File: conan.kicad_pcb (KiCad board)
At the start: 4 copper layers, 313 parts, among them J1 JST-XH, J10 PWM11, J11 PWM3, J12 PWM7, J13 PWM12, J14 PWM4, J15 PWM8, J16 Stepper, J17 Stepper, J18 Stepper, J19 Stepper, J2 JST-XH, J20 Stepper, J21 Stepper, J22 Boot, J23 UART1, J24 UART2, J25 USB_B_Micro, J26 Endstop 1, J27 Endstop 2, J28 Endstop 3, J29 Endstop 4, J3 JTAG, J30 Endstop 5, J31 Endstop 6, J32 Endstop 7, J33 Endstop 8, J34 Watchdog, J35 Thermistor 1, J36 Thermistor 2, J37 Thermistor 3, J38 Thermistor 4, J39 Thermistor 5, J4 PWM9, J40 Thermistor 6, J43 pmod, J44 esp8266, J45 Chain_in, J46 Chain_out, J47 Exp1_L, J48 Display, J49 Exp1_R, J5 PWM5, J50 Vaux in, J51 VM2 in, J52 VM1 in, J53 Vaux in, J54 Exp2_L, J55 Exp2_R, J6 PWM1_HP, J7 PWM10, J8 PWM2_HP, J9 PWM6, Q1 AON7524, Q2 TPH1R405PL, Q3 TPH1R405PL, Q4 AON7524, Q5 AON7524, Q6 AON7524, Q7 AON7524, Q8 AON7524, Q9 Q_NMOS_DGS, SW1 Reset, U1 ECP5U12_CABGA256, U10 TMC2209, U11 TMC2209, U12 TMC2209, U13 TMC2209, U14 AT25xxx, U15 STM32F070CBTx, U16 74VLX244, U17 STWD100, U2 L7986, U3 TLV62569, U4 TLV62569, U5 LP5907MFX-2.5, U6 LP5907MFX-3.3, U7 MIC4127, U8 TMC2209, U9 TMC2209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

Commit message: placement roughly done
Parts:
- J44: value esp8266 -> ESP8266
- Y1: value 8MHz -> 16MHz; footprint arne:crystal_ecs-5px -> Crystal:Crystal_SMD_SeikoEpson_TSX3225-4Pin_3.2x2.5mm
- moved J34 173.3 mm to (194.8, 28.2), turned to 180 degrees
- moved Q9 126.6 mm to (186.6, 26.7), turned to 270 degrees
- moved R65 120.1 mm to (185.7, 30.4), turned to 0 degrees
- moved R66 116.3 mm to (181.1, 31.0), turned to 0 degrees
- moved R67 113.1 mm to (181.6, 27.4), turned to 180 degrees
- moved U17 110.2 mm to (180.5, 35.5), turned to 0 degrees
- moved TH2 75.9 mm to (88.3, 36.4)
- moved TH1 75.9 mm to (164.2, 36.4)
- moved R56 63.0 mm to (65.8, 52.6)
- moved R55 61.9 mm to (62.8, 52.7)
- moved J25 61.1 mm to (53.8, 60.0), turned to 270 degrees
- moved R83 58.1 mm to (97.7, 63.7), turned to 90 degrees
- moved U15 58.0 mm to (66.7, 59.7), turned to 180 degrees
- moved R50 56.0 mm to (73.8, 62.1), turned to 270 degrees
- moved J23 55.7 mm to (82.3, 82.8), turned to 270 degrees
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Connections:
- J44 pad 2: ESP_EN -> GND
- J44 pad 3: ESP_RST -> ESP_EN
- J44 pad 4: +3V3 -> ESP_GPIO2
- J44 pad 5: ESP_RX -> ESP_RST
- J44 pad 7: ESP_GPIO2 -> +3V3
- J44 pad 8: GND -> ESP_RX
- U1 pad A13: CLK_50MHz -> display3
- U1 pad A7: display3 -> CLK_50MHz
- U1 pad C8: Net-(U1-PadC8) -> CLK_48MHz
- U15 pad 29: Net-(U15-Pad29) -> CLK_48MHz
- Y1 pad 2: Net-(C88-Pad1) -> GND
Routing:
- net CLK: track 135.9 -> 191.9 mm, vias 9 -> 10
- net DIR1: track 17.3 -> 73.2 mm
- net STEP1: track 17.7 -> 72.6 mm
- net INDEX1: track 19.3 -> 72.2 mm, vias 2 -> 3
- net DIAG1: track 18.0 -> 70.8 mm, vias 1 -> 2
- net ENN: track 177.8 -> 230.4 mm
- net UART2: track 3.77 -> 54.9 mm, vias 1 -> 2
- net DIR2: track 19.5 -> 69.8 mm, vias 2 -> 3
- net UART1: track 3.17 -> 52.4 mm, vias 0 -> 1
- net ADC6: track 13.8 -> 61.7 mm, vias 1 -> 2
- net exp2_17: track 2.20 -> 48.1 mm
- net exp2_16: track 3.33 -> 47.6 mm
- net exp2_14: track 4.90 -> 47.6 mm
- net exp2_15: track 2.20 -> 44.9 mm
- net exp2_13: track 2.20 -> 44.2 mm
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
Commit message: routing snapshot
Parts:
- moved R12 7.28 mm to (122.3, 57.4)
- moved X1 5.56 mm to (126.2, 56.5), turned to 180 degrees
- moved J48 2.45 mm to (111.1, 49.1)
- moved C49 1.05 mm to (126.2, 53.7), turned to 180 degrees
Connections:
- U1 pad A7: CLK_50MHz -> CLK_48MHz
- U1 pad C8: CLK_48MHz -> CLK_50MHz
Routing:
- net display6: track 3.17 -> 44.6 mm
- net display2: track 3.17 -> 24.0 mm
- net display8: track 4.73 -> 25.0 mm
- net display10: track 2.20 -> 21.8 mm
- net display4: track 3.77 -> 23.2 mm
- net display12: track 4.73 -> 23.8 mm
- net CLK_48MHz: track 3.91 -> 21.2 mm, vias 0 -> 2
- net display9: track 2.20 -> 19.1 mm
- net display7: track 3.77 -> 20.6 mm
- net display1: track 2.20 -> 19.0 mm
- net display3: track 2.20 -> 18.8 mm
- net display11: track 3.17 -> 19.4 mm
- net display5: track 4.73 -> 21.0 mm
- net display13: track 3.77 -> 19.5 mm
- net CLK_50MHz: track 2.20 -> 16.8 mm
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
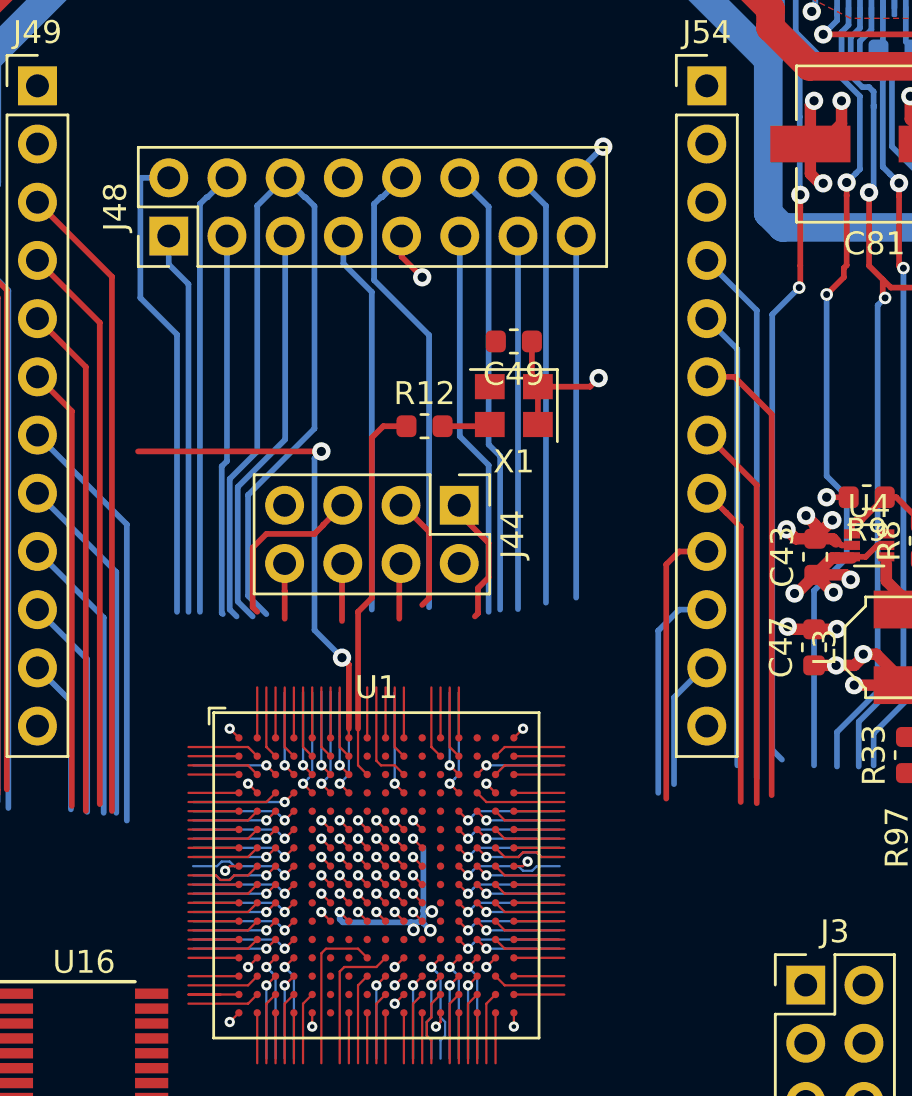
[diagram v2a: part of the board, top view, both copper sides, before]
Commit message: reassign some FPGA pins for ease of routing
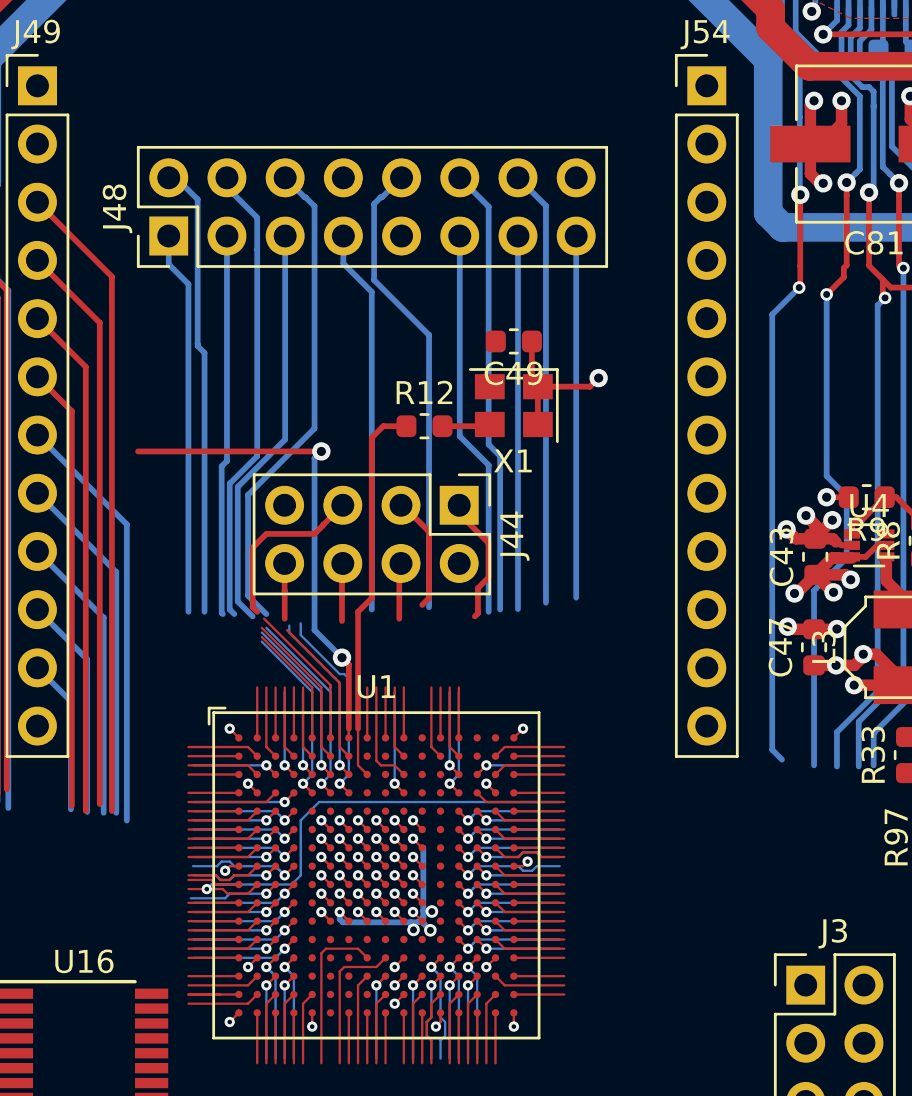
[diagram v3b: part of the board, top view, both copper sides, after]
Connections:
- U1 pad A10: chain_in_in3 -> ESP_TX
- U1 pad A12: ESP_FLASH -> display10
- U1 pad A13: display3 -> exp2_1
- U1 pad A5: display10 -> display2
- U1 pad A6: display9 -> display5
- U1 pad A8: display1 -> ESP_FLASH
- U1 pad A9: chain_in_in1 -> ESP_GPIO2
- U1 pad B10: chain_in_in2 -> ESP_EN
- U1 pad B12: ESP_GPIO2 -> display9
- U1 pad B13: ESP_EN -> display11
- U1 pad B15: exp2_12 -> exp2_2
- U1 pad B16: exp2_13 -> exp2_3
- U1 pad B5: display11 -> Net-(U1-PadB5)
- U1 pad B6: display6 -> display3
- U1 pad B7: display2 -> ESP_RST
- U1 pad C10: chain_in_out1 -> display7
- U1 pad C13: ESP_RX -> display12
- U1 pad C14: exp2_11 -> exp2_5
- U1 pad C15: exp2_7 -> exp2_4
- U1 pad C16: exp2_9 -> exp2_6
- U1 pad C5: display13 -> Net-(U1-PadC5)
- U1 pad C6: display7 -> Net-(U1-PadC6)
- U1 pad C7: display4 -> display6
- U1 pad D10: chain_in_out2 -> display8
- U1 pad D13: ESP_RST -> display13
- U1 pad D14: exp2_10 -> exp2_8
- U1 pad D16: exp2_5 -> exp2_7
- U1 pad D5: display12 -> display1
- U1 pad D6: display8 -> display4
- U1 pad D7: display5 -> ESP_RX
- U1 pad E13: ESP_TX -> STEP4
- U1 pad E14: exp2_8 -> INDEX4
- U1 pad E15: exp2_3 -> DIAG4
- U1 pad E16: DIAG6 -> DIR4
- U1 pad F13: exp2_4 -> Net-(U1-PadF13)
- U1 pad F14: exp2_6 -> Net-(U1-PadF14)
- U1 pad F15: exp2_2 -> Net-(U1-PadF15)
- U1 pad G13: exp2_1 -> Net-(U1-PadG13)
- U1 pad H14: DIAG4 -> Net-(U1-PadH14)
- U1 pad J13: INDEX4 -> Net-(U1-PadJ13)
- U1 pad J15: DIR4 -> Net-(U1-PadJ15)
- U1 pad K15: STEP4 -> Net-(U1-PadK15)
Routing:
- net exp2_1: track 28.2 -> 2.20 mm, vias 1 -> 0
- net exp2_3: track 23.3 -> 2.20 mm
- net exp2_2: track 23.2 -> 3.17 mm
- net exp2_4: track 21.7 -> 3.17 mm, vias 1 -> 0
- net CLK: track 191.9 -> 210.4 mm, vias 10 -> 11
- net display6: track 44.6 -> 28.7 mm, vias 0 -> 1
- net exp2_6: track 16.0 -> 2.20 mm, vias 1 -> 0
- net exp2_5: track 16.3 -> 3.77 mm, vias 0 -> 1
- net exp2_7: track 12.7 -> 2.20 mm
- net Net-(U1-PadC6): track 0.00 -> 7.44 mm, vias 0 -> 1
- net display1: track 19.0 -> 24.6 mm, vias 0 -> 1
- net display4: track 23.2 -> 28.9 mm
- net exp2_8: track 9.49 -> 3.97 mm, vias 1 -> 0
- net ESP_RX: track 6.18 -> 11.1 mm
- net Net-(U1-PadG13): track 0.00 -> 4.73 mm, vias 0 -> 1
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
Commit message: more routing
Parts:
- moved R45 29.5 mm to (161.9, 51.9)
- moved R97 24.2 mm to (147.7, 51.4)
- moved R48 24.1 mm to (150.4, 51.4)
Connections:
- U1 pad A5: display2 -> display1
- U1 pad C6: Net-(U1-PadC6) -> display2
- U1 pad D5: display1 -> Net-(U1-PadD5)
- U1 pad J2: CLK -> exp1_12
- U1 pad J4: exp1_12 -> CLK
- U1 pad K2: ENN -> PWM5
- U1 pad K4: PWM5 -> ENN
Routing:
- net UART6: track 4.90 -> 49.6 mm, vias 1 -> 2
- net ENN: track 230.4 -> 266.7 mm, vias 10 -> 13
- net UART5: track 2.20 -> 36.2 mm, vias 0 -> 1
- net Net-(R45-Pad2): track 48.6 -> 19.0 mm, vias 4 -> 3
- net exp2_1: track 2.20 -> 25.3 mm
- net Net-(R48-Pad2): track 37.6 -> 15.1 mm, vias 4 -> 3
- net Net-(R97-Pad2): track 42.7 -> 20.4 mm, vias 4 -> 3
- net exp2_2: track 3.17 -> 23.3 mm
- net UART4: track 3.77 -> 23.3 mm, vias 1 -> 2
- net exp2_3: track 2.20 -> 20.3 mm
- net STEP6: track 52.0 -> 69.1 mm
- net exp2_4: track 3.17 -> 20.2 mm
- net DIAG6: track 49.5 -> 66.4 mm
- net DIR6: track 54.3 -> 71.1 mm
- net INDEX6: track 50.3 -> 66.9 mm
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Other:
- net class Default: clearance 0.1 -> 0.15
- rule trace_clearance: 0.1 -> 0.15

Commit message: more routing
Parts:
- Q1: footprint Package_DFN_QFN:DFN-8-1EP_3x3mm_P0.5mm_EP1.66x2.38mm -> arne:FET_DGS_DFN3x3A_8L_EP1_P
- moved R95 87.4 mm to (196.6, 86.8)
- moved R86 80.1 mm to (117.2, 90.7)
- moved R25 10.4 mm to (134.3, 93.4), turned to 90 degrees
- moved J3 9.58 mm to (132.2, 88.5), turned to 90 degrees
- moved JP3 9.08 mm to (165.3, 88.0), turned to 270 degrees
- moved R13 7.27 mm to (161.4, 91.5), turned to 90 degrees
- moved JP2 6.59 mm to (123.1, 93.0)
- moved R29 5.75 mm to (185.2, 76.4), turned to 90 degrees
- moved JP4 5.51 mm to (142.3, 93.0)
- moved R19 5.37 mm to (171.6, 92.2), turned to 90 degrees
- moved R21 4.73 mm to (176.4, 73.8), turned to 0 degrees
- moved R17 4.44 mm to (130.8, 93.4), turned to 90 degrees
- moved R30 4.32 mm to (189.3, 92.3), turned to 90 degrees
- moved R28 4.26 mm to (150.7, 93.5), turned to 90 degrees
- moved J10 4.15 mm to (146.7, 98.6), turned to 180 degrees
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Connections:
- U1 pad F13: Net-(U1-PadF13) -> DIR5
- U1 pad F14: Net-(U1-PadF14) -> INDEX5
- U1 pad F15: Net-(U1-PadF15) -> STEP5
- U1 pad F16: INDEX6 -> UART5
- U1 pad G13: Net-(U1-PadG13) -> UART6
- U1 pad G14: DIAG5 -> STEP6
- U1 pad G15: INDEX5 -> DIR6
- U1 pad G16: UART5 -> DIAG5
- U1 pad H13: UART6 -> INDEX6
- U1 pad H14: Net-(U1-PadH14) -> exp2_17
- U1 pad H15: DIR6 -> DIAG6
- U1 pad J13: Net-(U1-PadJ13) -> exp2_12
- U1 pad J15: Net-(U1-PadJ15) -> exp2_15
- U1 pad J16: DIR5 -> exp2_16
- U1 pad K13: pmod1_4 -> exp2_11
- U1 pad K14: STEP6 -> exp2_10
- U1 pad K15: Net-(U1-PadK15) -> exp2_13
- U1 pad K16: STEP5 -> exp2_14
- U1 pad L1: PWM1 -> Net-(U1-PadL1)
- U1 pad L13: pmod1_3 -> exp2_9
- U1 pad L14: pmod1_1 -> PWM2
- U1 pad L16: pmod2_1 -> PWM1
- U1 pad M1: PWM2 -> Net-(U1-PadM1)
- U1 pad N12: exp2_14 -> Net-(U1-PadN12)
- U1 pad R12: exp2_16 -> Net-(U1-PadR12)
- U1 pad T13: exp2_15 -> Net-(U1-PadT13)
- U1 pad T14: exp2_17 -> Net-(U1-PadT14)
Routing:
- net PWM2: track 5.41 -> 75.8 mm, vias 0 -> 2
- net PWM1: track 5.49 -> 72.4 mm, vias 0 -> 2
- net PWM4: track 3.17 -> 52.1 mm, vias 0 -> 2
- net +3V3: track 35.2 -> 83.6 mm, vias 24 -> 26
- net PWM3: track 3.17 -> 42.6 mm, vias 0 -> 2
- net exp2_11: track 38.5 -> 70.7 mm, vias 0 -> 1
- net exp2_9: track 35.8 -> 67.5 mm, vias 0 -> 1
- net exp2_12: track 40.7 -> 72.1 mm, vias 0 -> 1
- net exp2_10: track 36.3 -> 67.5 mm, vias 0 -> 1
- net exp2_13: track 42.0 -> 71.7 mm, vias 0 -> 1
- net exp2_15: track 44.9 -> 74.0 mm, vias 0 -> 1
- net GND: track 291.2 -> 320.0 mm, vias 119 -> 142
- net exp2_16: track 47.6 -> 74.0 mm, vias 0 -> 1
- net exp2_14: track 47.6 -> 72.0 mm
- net +2V5: track 35.1 -> 15.2 mm, vias 10 -> 7
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- added copper zone on In1.Cu, net GND
- added copper zone on In2.Cu, net Net-(J10-Pad3)
- added copper zone on F.Cu, net Net-(J11-Pad1)
- added copper zone on F.Cu, net Net-(J12-Pad1)
- added copper zone on In2.Cu, net Net-(J12-Pad2)
- added copper zone on F.Cu, net Net-(J14-Pad1)
- added copper zone on F.Cu, net Net-(J15-Pad1)
- added copper zone on In2.Cu, net Net-(J4-Pad3)
- added copper zone on F.Cu, net Net-(J5-Pad1)
- added copper zone on F.Cu, net Net-(J9-Pad1)

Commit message: power routing done
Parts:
- C48: moved to B.Cu
- moved R11 40.2 mm to (72.1, 64.8)
- moved R10 39.4 mm to (75.4, 64.8)
- moved J35 38.0 mm to (61.7, 77.5)
- moved J40 37.8 mm to (99.5, 77.5)
- moved J24 35.2 mm to (54.6, 52.0), turned to 180 degrees
- moved J23 29.9 mm to (54.5, 71.9), turned to 180 degrees
- moved R53 26.2 mm to (50.2, 49.9)
- moved J36 23.0 mm to (69.2, 77.5)
- moved JP11 22.6 mm to (74.6, 92.3), turned to 270 degrees
- moved J39 22.6 mm to (91.8, 77.5)
- moved R54 21.6 mm to (51.0, 53.3)
- moved C48 17.4 mm to (71.4, 59.5), turned to 270 degrees
- moved R88 13.0 mm to (57.8, 80.6)
- moved R92 12.5 mm to (107.4, 91.1), turned to 90 degrees
- moved R89 12.5 mm to (57.8, 82.7)
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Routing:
- net +3V3: track 83.6 -> 180.1 mm, vias 26 -> 38
- net Net-(J26-Pad1): track 0.00 -> 86.4 mm
- net +5V: track 47.6 -> 124.9 mm, vias 14 -> 22
- net CLK_48MHz: track 21.2 -> 86.1 mm, vias 2 -> 6
- net WDEN: track 2.20 -> 65.8 mm, vias 0 -> 2
- net WDI: track 2.28 -> 60.2 mm, vias 0 -> 2
- net chain_out_in2: track 3.17 -> 58.3 mm
- net chain_out_in1: track 3.77 -> 58.5 mm
- net chain_out_out1: track 2.20 -> 55.5 mm, vias 0 -> 1
- net Net-(J30-Pad3): track 0.00 -> 51.8 mm
- net chain_out_out2: track 4.73 -> 56.2 mm, vias 1 -> 2
- net chain_out_out3: track 2.20 -> 53.0 mm, vias 0 -> 1
- net Net-(J26-Pad3): track 0.00 -> 50.6 mm
- net FPGA2: track 4.73 -> 54.3 mm, vias 1 -> 2
- net FPGA3: track 3.60 -> 51.9 mm, vias 0 -> 1
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- added copper zone on F.Cu, net Net-(J34-Pad1)
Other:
- net class Default: clearance 0.15 -> 0.1
- rule trace_clearance: 0.15 -> 0.1

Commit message: more routing
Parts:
- added REF**: MountingHole_3.2mm_M3, MountingHole:MountingHole_3.2mm_M3, F.Cu at (200.9, 97.5)
- added REF**: MountingHole_3.2mm_M3, MountingHole:MountingHole_3.2mm_M3, F.Cu at (54.4, 97.5)
- added REF**: MountingHole_3.2mm_M3, MountingHole:MountingHole_3.2mm_M3, F.Cu at (54.4, 27.7)
- added REF**: MountingHole_3.2mm_M3, MountingHole:MountingHole_3.2mm_M3, F.Cu at (119.7, 41.0)
- added REF**: MountingHole_3.2mm_M3, MountingHole:MountingHole_3.2mm_M3, F.Cu at (200.9, 27.7)
- moved R75 95.9 mm to (193.3, 29.5)
- moved D11 95.4 mm to (193.4, 26.0)
- moved C1 79.2 mm to (128.0, 7.49)
- moved C10 79.2 mm to (124.0, 8.47)
- moved C13 79.2 mm to (119.4, 13.6)
- moved C18 79.2 mm to (128.0, 11.1)
- moved C20 79.2 mm to (122.5, 18.2)
- moved C22 79.2 mm to (124.0, 11.6)
- moved C23 79.2 mm to (117.9, 19.2)
- moved C25 79.2 mm to (123.0, 14.6)
- moved C4 79.2 mm to (119.9, 10.0)
- moved C7 79.2 mm to (118.4, 16.1)
- moved R72 59.6 mm to (183.7, 57.7), turned to 270 degrees
- moved R69 58.8 mm to (113.7, 58.9), turned to 180 degrees
- moved D5 53.5 mm to (112.7, 61.8), turned to 90 degrees
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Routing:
- net LED8: track 2.20 -> 99.3 mm, vias 0 -> 2
- net +3V3: track 180.1 -> 237.3 mm, vias 38 -> 42
- net LED5: track 3.17 -> 55.0 mm, vias 0 -> 1
- net /mcu/TX: track 0.00 -> 28.0 mm, vias 0 -> 1
- net Net-(R53-Pad1): track 0.00 -> 22.0 mm, vias 0 -> 2
- net Net-(C89-Pad1): track 16.9 -> 37.3 mm, vias 0 -> 2
- net LED4: track 3.17 -> 19.6 mm
- net Net-(D8-Pad2): track 0.00 -> 15.8 mm, vias 0 -> 2
- net Net-(J23-Pad2): track 0.00 -> 13.4 mm, vias 0 -> 2
- net Net-(J23-Pad3): track 0.00 -> 12.9 mm, vias 0 -> 2
- net GND: track 366.5 -> 377.8 mm, vias 164 -> 166
- net Net-(R55-Pad2): track 2.25 -> 10.3 mm
- net LED3: track 3.77 -> 11.7 mm
- net /mcu/RX: track 0.00 -> 7.85 mm
- net LED6: track 2.20 -> 9.01 mm
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
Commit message: more routing
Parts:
- removed C10, C11, C13, C16, C19, C8: 10nF, Capacitor_SMD:C_0603_1608Metric
- removed C28, C31, C33, C34, C9, C95: 100nF, Capacitor_SMD:C_0603_1608Metric
- removed REF** (x5): MountingHole_3.2mm_M3, MountingHole:MountingHole_3.2mm_M3
- added H1: MountingHole, MountingHole:MountingHole_3.2mm_M3, F.Cu at (54.4, 27.9)
- added H2: MountingHole, MountingHole:MountingHole_3.2mm_M3, F.Cu at (200.9, 27.9)
- added H3: MountingHole, MountingHole:MountingHole_3.2mm_M3, F.Cu at (54.4, 97.5)
- added H4: MountingHole, MountingHole:MountingHole_3.2mm_M3, F.Cu at (200.9, 97.5)
- added H5: MountingHole, MountingHole:MountingHole_3.2mm_M3, F.Cu at (119.7, 41.0)
- C1, C14, C15, C18, C2, C20, C21, C22, C23, C24, C25, C26, C27, C3, C30, C35, C4, C5, C6, C7: footprint Capacitor_SMD:C_0603_1608Metric -> Capacitor_SMD:C_0402_1005Metric; moved to B.Cu
- C12, C17, C36, C92, C93, C94, C96, C97: moved to B.Cu
- moved C36 96.5 mm to (126.4, 71.0), turned to 90 degrees
- moved C24 95.6 mm to (118.6, 73.8)
- moved C14 95.3 mm to (121.9, 72.5), turned to 90 degrees
- moved C17 95.2 mm to (127.9, 81.7), turned to 270 degrees
- moved C2 93.7 mm to (123.3, 77.9), turned to 270 degrees
- moved C5 93.2 mm to (123.3, 76.0), turned to 270 degrees
- moved C12 92.5 mm to (125.9, 81.5), turned to 270 degrees
- moved C26 90.8 mm to (120.6, 73.8), turned to 180 degrees
- moved C21 90.3 mm to (117.0, 74.2), turned to 90 degrees
- moved C30 89.8 mm to (120.0, 72.4), turned to 180 degrees
- moved C15 88.3 mm to (123.3, 79.8), turned to 270 degrees
- moved C6 87.7 mm to (121.8, 80.6), turned to 270 degrees
- moved C35 87.6 mm to (113.8, 82.2), turned to 270 degrees
- moved C27 87.1 mm to (113.7, 71.9), turned to 90 degrees
- moved C3 82.0 mm to (118.0, 79.7), turned to 180 degrees
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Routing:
- net +3V3: track 237.3 -> 268.3 mm, vias 42 -> 52
- net GND: track 377.8 -> 408.0 mm, vias 166 -> 181
- net +1V1: track 17.7 -> 24.3 mm, vias 9 -> 12
- net +2V5: track 15.2 -> 20.3 mm, vias 7 -> 8
- net Net-(J23-Pad2): track 13.4 -> 18.0 mm
- net Net-(J23-Pad3): track 12.9 -> 15.7 mm
- net Net-(D3-Pad1): track 16.8 -> 19.3 mm
- net exp1_1: track 50.9 -> 51.5 mm
